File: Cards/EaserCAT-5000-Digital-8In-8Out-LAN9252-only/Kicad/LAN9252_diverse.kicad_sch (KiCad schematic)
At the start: 41 parts, among them CN1 10pF, CN2 10pF, CN3 0.1uF, CN4 0.1uF, J8 Conn_01x02_Pin, U6 AT24CS32-SSHM, U7 AMS1117-3.3

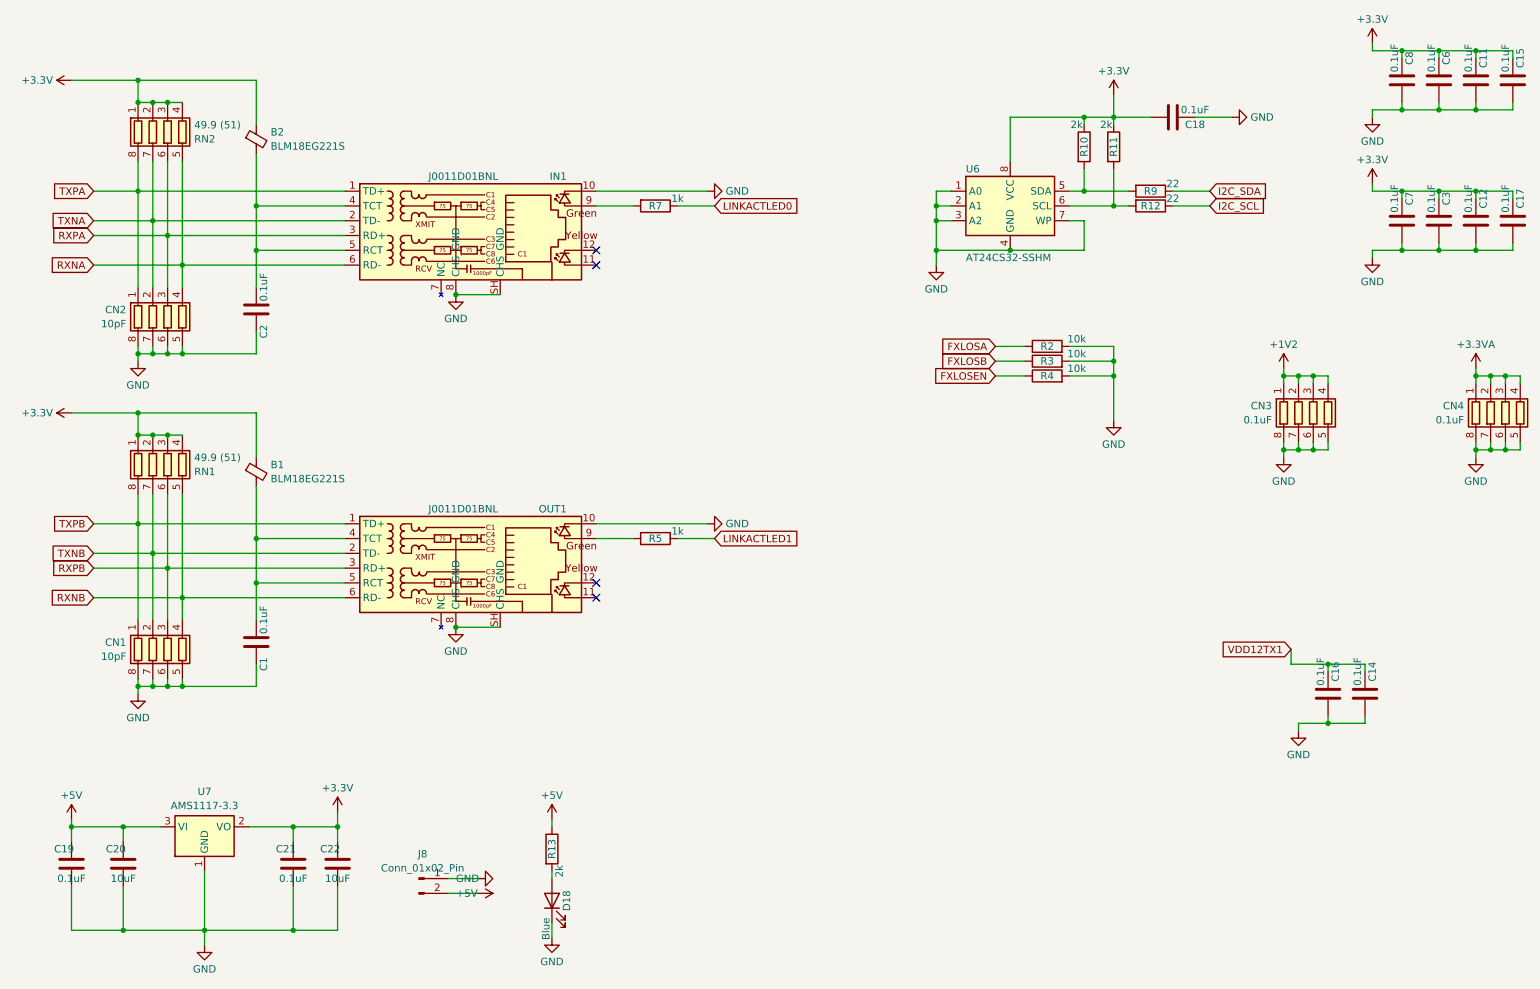
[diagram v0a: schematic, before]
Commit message: Updated 24V field voltage routing. Files sent for fab
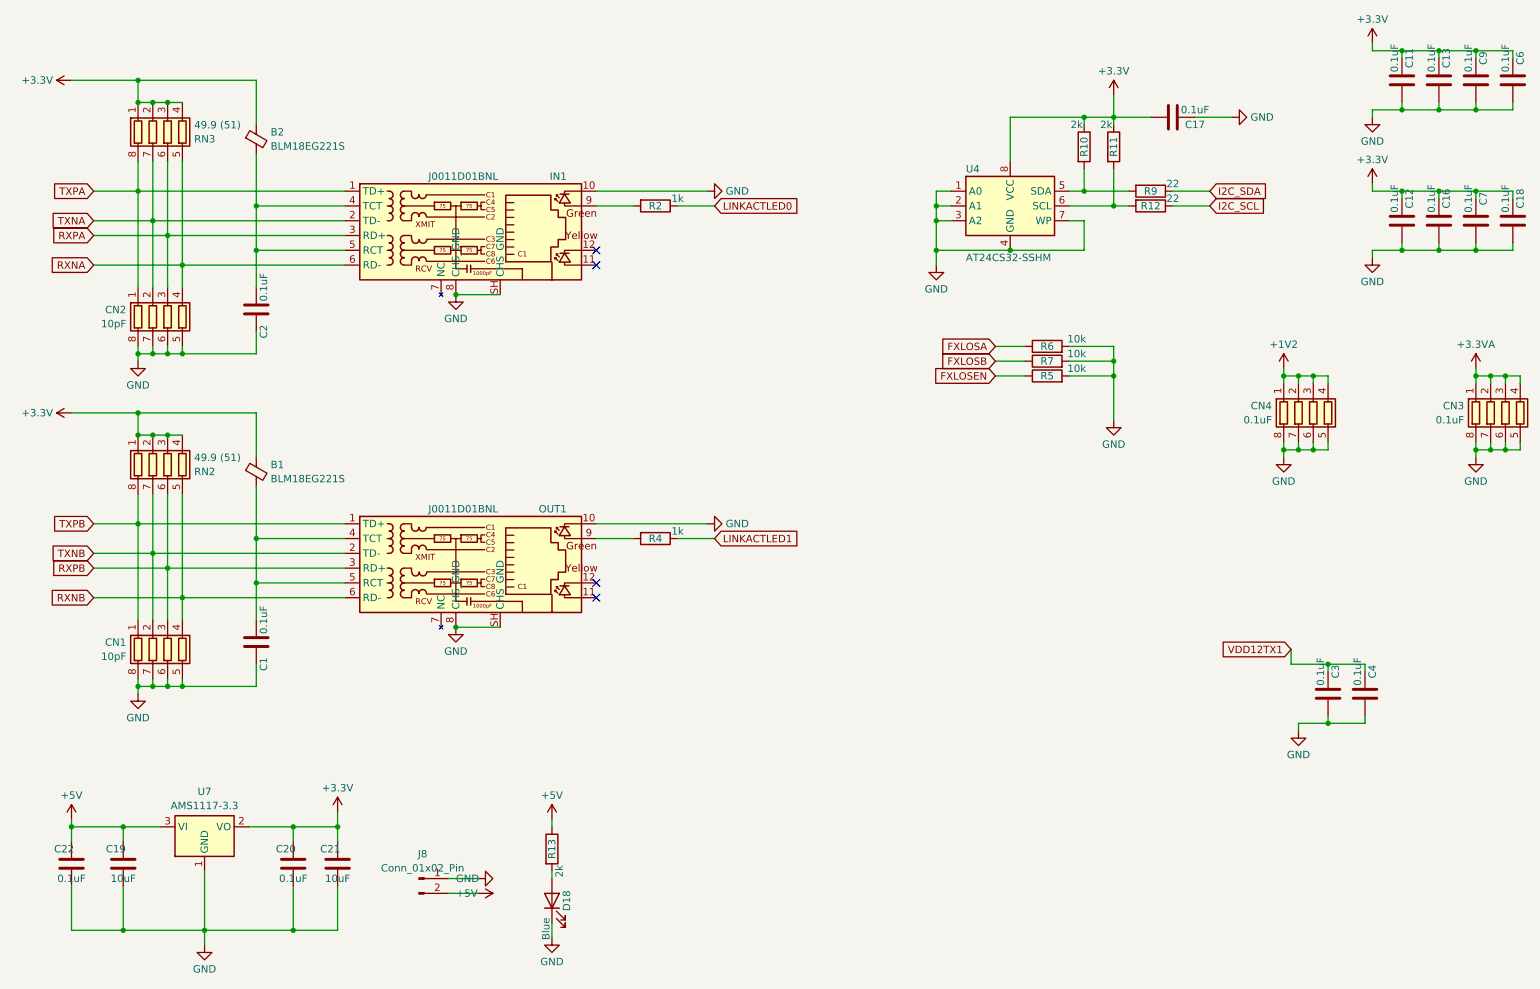
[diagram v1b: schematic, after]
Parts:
- renumbered C8 to C11, C7 to C12, C6 to C13, C3 to C16, C18 to C17, C17 to C18, C20 to C19, C21 to C20, C22 to C21, C19 to C22, C16 to C3, C14 to C4, C15 to C6, C12 to C7, C11 to C9, CN4 to CN3, CN3 to CN4, R7 to R2, R5 to R4, R4 to R5, R2 to R6, R3 to R7, RN1 to RN2, RN2 to RN3, U6 to U4
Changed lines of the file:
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@@
 		(on_board yes)
 		(dnp no)
-		(property "Reference" "U6"
+		(property "Reference" "U4"
 			(at 182.88 43.18 0)
 			(effects
@@
 			(project "THCAD-reader"
 				(path "/5597aedc-b607-407f-bbfd-31b3b298ecb1/650f1ee4-2ce7-4e9d-a70d-f9d8defa5d03"
-					(reference "U6")
+					(reference "U4")
 					(unit 1)
 				)
@@
 		(on_board yes)
 		(dnp no)
-		(property "Reference" "CN4"
+		(property "Reference" "CN3"
 			(at 268.478 83.8778 0)
 			(effects
@@
 			(project "8In-8Out-LAN9252-only"
 				(path "/5597aedc-b607-407f-bbfd-31b3b298ecb1/650f1ee4-2ce7-4e9d-a70d-f9d8defa5d03"
-					(reference "CN4")
+					(reference "CN3")
 					(unit 1)
 				)
@@
 		(on_board yes)
 		(dnp no)
-		(property "Reference" "RN1"
+		(property "Reference" "RN2"
 			(at 50.292 95.1922 0)
 			(effects
@@
 			(project "8In-8Out-LAN9252-only"
 				(path "/5597aedc-b607-407f-bbfd-31b3b298ecb1/650f1ee4-2ce7-4e9d-a70d-f9d8defa5d03"
-					(reference "RN1")
+					(reference "RN2")
 					(unit 1)
 				)
@@
 		(on_board yes)
 		(dnp no)
-		(property "Reference" "R2"
+		(property "Reference" "R6"
 			(at 196.85 73.66 90)
 			(effects
@@
 			(project "THCAD-reader"
 				(path "/5597aedc-b607-407f-bbfd-31b3b298ecb1/650f1ee4-2ce7-4e9d-a70d-f9d8defa5d03"
-					(reference "R2")
+					(reference "R6")
 					(unit 1)
 				)
@@
 		(on_board yes)
 		(dnp no)
-		(property "Reference" "C17"
+		(property "Reference" "C18"
 			(at 278.13 48.26 90)
 			(effects
@@
 			(project "THCAD-reader"
 				(path "/5597aedc-b607-407f-bbfd-31b3b298ecb1/650f1ee4-2ce7-4e9d-a70d-f9d8defa5d03"
-					(reference "C17")
+					(reference "C18")
 					(unit 1)
 				)
@@
 		(on_board yes)
 		(dnp no)
-		(property "Reference" "C11"
+		(property "Reference" "C9"
 			(at 271.78 24.13 90)
 			(effects
@@
 			(project "THCAD-reader"
 				(path "/5597aedc-b607-407f-bbfd-31b3b298ecb1/650f1ee4-2ce7-4e9d-a70d-f9d8defa5d03"
-					(reference "C11")
+					(reference "C9")
 					(unit 1)
 				)
@@
 		(on_board yes)
 		(dnp no)
-		(property "Reference" "C8"
+		(property "Reference" "C11"
 			(at 259.08 24.13 90)
 			(effects
@@
 			(project "THCAD-reader"
 				(path "/5597aedc-b607-407f-bbfd-31b3b298ecb1/650f1ee4-2ce7-4e9d-a70d-f9d8defa5d03"
-					(reference "C8")
+					(reference "C11")
 					(unit 1)
 				)
@@
 		(on_board yes)
 		(dnp no)
-		(property "Reference" "R3"
+		(property "Reference" "R7"
 			(at 196.85 76.2 90)
 			(effects
@@
 			(project "THCAD-reader"
 				(path "/5597aedc-b607-407f-bbfd-31b3b298ecb1/650f1ee4-2ce7-4e9d-a70d-f9d8defa5d03"
-					(reference "R3")
+					(reference "R7")
 					(unit 1)
 				)
@@
 		(on_board yes)
 		(dnp no)
-		(property "Reference" "R5"
+		(property "Reference" "R4"
 			(at 129.54 106.68 90)
 			(effects
@@
 			(project "8In-8Out-LAN9252-only"
 				(path "/5597aedc-b607-407f-bbfd-31b3b298ecb1/650f1ee4-2ce7-4e9d-a70d-f9d8defa5d03"
-					(reference "R5")
+					(reference "R4")
 					(unit 1)
 				)
@@
 		(on_board yes)
 		(dnp no)
-		(property "Reference" "C20"
+		(property "Reference" "C19"
 			(at 36.83 160.02 0)
 			(effects
@@
 			(project "8In-8Out-LAN9252-only"
 				(path "/5597aedc-b607-407f-bbfd-31b3b298ecb1/650f1ee4-2ce7-4e9d-a70d-f9d8defa5d03"
-					(reference "C20")
+					(reference "C19")
 					(unit 1)
 				)
@@
 		(on_board yes)
 		(dnp no)
-		(property "Reference" "C14"
+		(property "Reference" "C4"
 			(at 252.73 129.54 90)
 			(effects
@@
 			(project "THCAD-reader"
 				(path "/5597aedc-b607-407f-bbfd-31b3b298ecb1/650f1ee4-2ce7-4e9d-a70d-f9d8defa5d03"
-					(reference "C14")
+					(reference "C4")
 					(unit 1)
 				)
@@
 		(on_board yes)
 		(dnp no)
-		(property "Reference" "C18"
+		(property "Reference" "C17"
 			(at 222.25 35.56 90)
 			(effects
@@
 			(project "THCAD-reader"
 				(path "/5597aedc-b607-407f-bbfd-31b3b298ecb1/650f1ee4-2ce7-4e9d-a70d-f9d8defa5d03"
-					(reference "C18")
+					(reference "C17")
 					(unit 1)
 				)
@@
 		(on_board yes)
 		(dnp no)
-		(property "Reference" "RN2"
+		(property "Reference" "RN3"
 			(at 50.292 38.0422 0)
 			(effects
@@
 			(project "8In-8Out-LAN9252-only"
 				(path "/5597aedc-b607-407f-bbfd-31b3b298ecb1/650f1ee4-2ce7-4e9d-a70d-f9d8defa5d03"
-					(reference "RN2")
+					(reference "RN3")
 					(unit 1)
 				)
@@
 		(on_board yes)
 		(dnp no)
-		(property "Reference" "R4"
+		(property "Reference" "R5"
 			(at 196.85 78.74 90)
 			(effects
@@
 			(project "THCAD-reader"
 				(path "/5597aedc-b607-407f-bbfd-31b3b298ecb1/650f1ee4-2ce7-4e9d-a70d-f9d8defa5d03"
-					(reference "R4")
+					(reference "R5")
 					(unit 1)
 				)
@@
 		(on_board yes)
 		(dnp no)
-		(property "Reference" "R7"
+		(property "Reference" "R2"
 			(at 129.54 49.53 90)
 			(effects
@@
 			(project "THCAD-reader"
 				(path "/5597aedc-b607-407f-bbfd-31b3b298ecb1/650f1ee4-2ce7-4e9d-a70d-f9d8defa5d03"
-					(reference "R7")
+					(reference "R2")
 					(unit 1)
 				)
@@
 		(on_board yes)
 		(dnp no)
-		(property "Reference" "C6"
+		(property "Reference" "C13"
 			(at 265.43 24.13 90)
 			(effects
@@
 			(project "THCAD-reader"
 				(path "/5597aedc-b607-407f-bbfd-31b3b298ecb1/650f1ee4-2ce7-4e9d-a70d-f9d8defa5d03"
-					(reference "C6")
+					(reference "C13")
 					(unit 1)
 				)
@@
 		(on_board yes)
 		(dnp no)
-		(property "Reference" "C12"
+		(property "Reference" "C7"
 			(at 271.78 48.26 90)
 			(effects
@@
 			(project "THCAD-reader"
 				(path "/5597aedc-b607-407f-bbfd-31b3b298ecb1/650f1ee4-2ce7-4e9d-a70d-f9d8defa5d03"
-					(reference "C12")
+					(reference "C7")
 					(unit 1)
 				)
@@
 		(on_board yes)
 		(dnp no)
-		(property "Reference" "C3"
+		(property "Reference" "C16"
 			(at 265.43 48.26 90)
 			(effects
@@
 			(project "THCAD-reader"
 				(path "/5597aedc-b607-407f-bbfd-31b3b298ecb1/650f1ee4-2ce7-4e9d-a70d-f9d8defa5d03"
-					(reference "C3")
+					(reference "C16")
 					(unit 1)
 				)
@@
 		(on_board yes)
 		(dnp no)
-		(property "Reference" "C22"
+		(property "Reference" "C21"
 			(at 73.66 160.02 0)
 			(effects
@@
 			(project "8In-8Out-LAN9252-only"
 				(path "/5597aedc-b607-407f-bbfd-31b3b298ecb1/650f1ee4-2ce7-4e9d-a70d-f9d8defa5d03"
-					(reference "C22")
+					(reference "C21")
 					(unit 1)
 				)
@@
 		(on_board yes)
 		(dnp no)
-		(property "Reference" "C16"
+		(property "Reference" "C3"
 			(at 246.38 129.54 90)
 			(effects
@@
 			(project "THCAD-reader"
 				(path "/5597aedc-b607-407f-bbfd-31b3b298ecb1/650f1ee4-2ce7-4e9d-a70d-f9d8defa5d03"
-					(reference "C16")
+					(reference "C3")
 					(unit 1)
 				)
@@
 		(on_board yes)
 		(dnp no)
-		(property "Reference" "C7"
+		(property "Reference" "C12"
 			(at 259.08 48.26 90)
 			(effects
@@
 			(project "THCAD-reader"
 				(path "/5597aedc-b607-407f-bbfd-31b3b298ecb1/650f1ee4-2ce7-4e9d-a70d-f9d8defa5d03"
-					(reference "C7")
+					(reference "C12")
 					(unit 1)
 				)
@@
 		(on_board yes)
 		(dnp no)
-		(property "Reference" "C19"
+		(property "Reference" "C22"
 			(at 27.94 160.02 0)
 			(effects
@@
 			(project "8In-8Out-LAN9252-only"
 				(path "/5597aedc-b607-407f-bbfd-31b3b298ecb1/650f1ee4-2ce7-4e9d-a70d-f9d8defa5d03"
-					(reference "C19")
+					(reference "C22")
 					(unit 1)
 				)
@@
 		(on_board yes)
 		(dnp no)
-		(property "Reference" "C21"
+		(property "Reference" "C20"
 			(at 66.04 160.02 0)
 			(effects
@@
 			(project "8In-8Out-LAN9252-only"
 				(path "/5597aedc-b607-407f-bbfd-31b3b298ecb1/650f1ee4-2ce7-4e9d-a70d-f9d8defa5d03"
-					(reference "C21")
+					(reference "C20")
 					(unit 1)
 				)
@@
 		(on_board yes)
 		(dnp no)
-		(property "Reference" "C15"
+		(property "Reference" "C6"
 			(at 278.13 24.13 90)
 			(effects
@@
 			(project "THCAD-reader"
 				(path "/5597aedc-b607-407f-bbfd-31b3b298ecb1/650f1ee4-2ce7-4e9d-a70d-f9d8defa5d03"
-					(reference "C15")
+					(reference "C6")
 					(unit 1)
 				)
@@
 		(on_board yes)
 		(dnp no)
-		(property "Reference" "CN3"
+		(property "Reference" "CN4"
 			(at 235.458 83.8778 0)
 			(effects
@@
 			(project "8In-8Out-LAN9252-only"
 				(path "/5597aedc-b607-407f-bbfd-31b3b298ecb1/650f1ee4-2ce7-4e9d-a70d-f9d8defa5d03"
-					(reference "CN3")
+					(reference "CN4")
 					(unit 1)
 				)

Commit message: Updates to hw straps after startup of card.
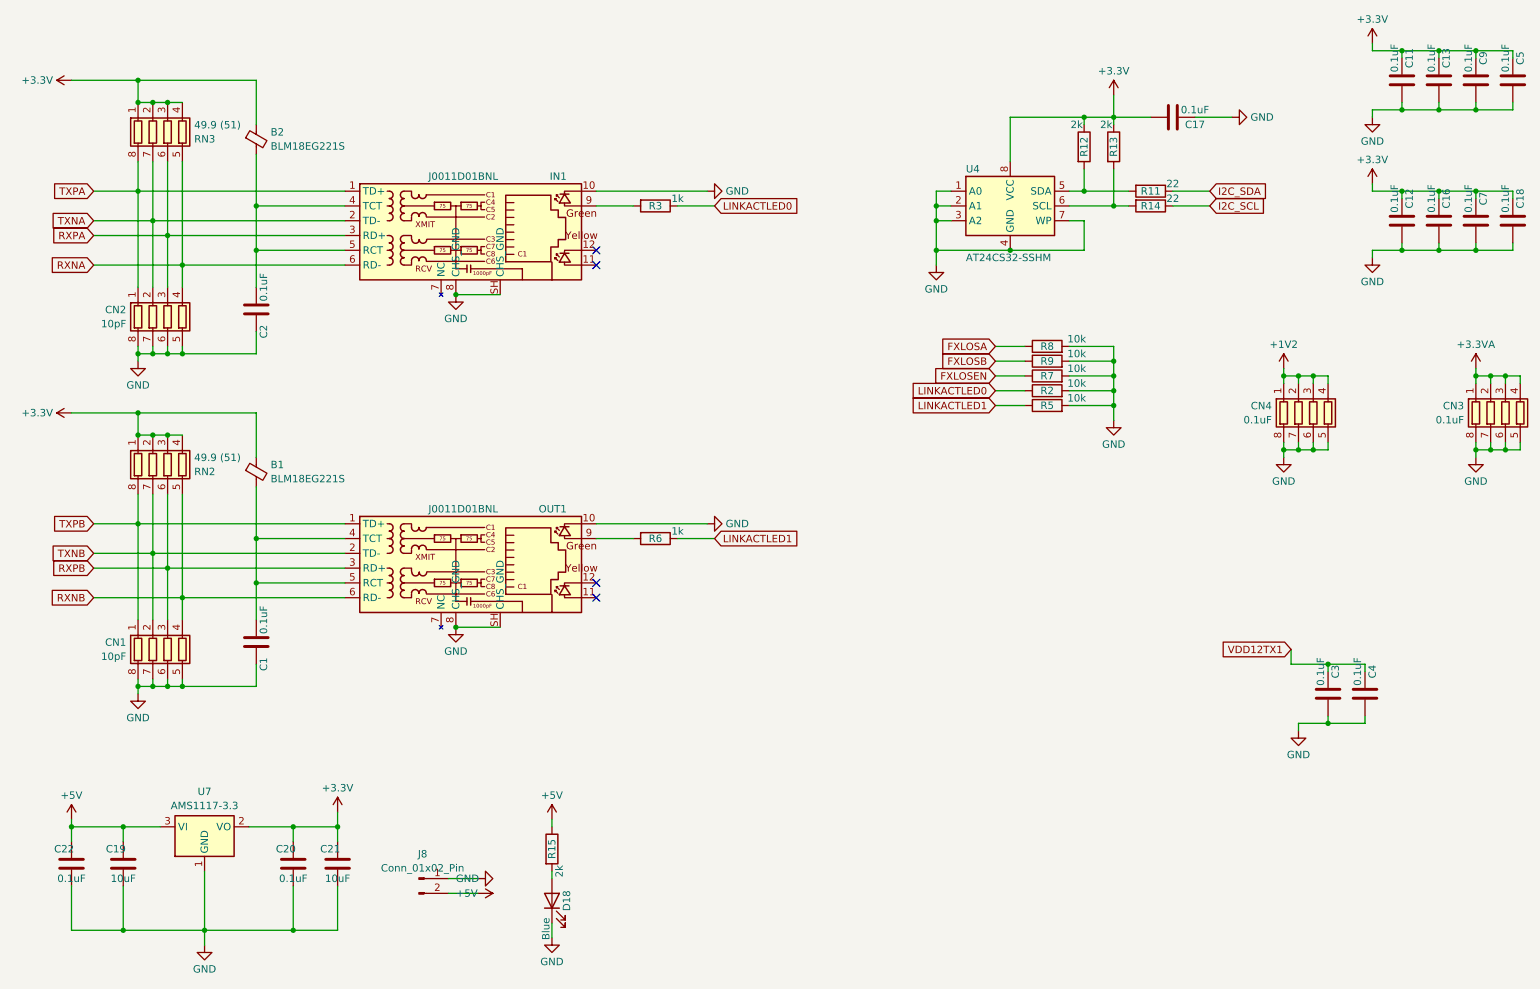
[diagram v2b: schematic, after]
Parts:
- added R2, R5: 10k, Resistor_SMD:R_0805_2012Metric, symbol Device:R
- renumbered C6 to C5, R9 to R11, R10 to R12, R11 to R13, R12 to R14, R13 to R15, R2 to R3, R4 to R6, R5 to R7, R6 to R8, R7 to R9
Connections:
- net GND: now also R2.2, R5.2
- net LINKACTLED0: now also R2.1
- net LINKACTLED1: now also R5.1
